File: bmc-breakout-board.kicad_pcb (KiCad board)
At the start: 4 copper layers, 90 x 60 mm, 49 parts, among them J1 PinHeader_2x4, J10 PinHeader_2x4, J11 PinHeader_2x05, J12 61300411121, J13 0473460001, J14 PCIE_BUS_x1, J15 0473460001, J16 PinHeader_1x07, J17 UE27AC54100, J2 PinHeader_2x13, J3 PinHeader_2x08, J4 61300411121, J5 ME1016813401101, J6 61300411121, J7 DC_SOCKET, J8 PinHeader_2x05, J9 PinHeader_1x07, Q1 SI2337DS, U1 FT234XD-R

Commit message: Bump revision to 1.0.1
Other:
- board text added: "DC-SCM Breakout Board Rev. 1.0.1"
- board text removed: "DC-SCM Breakout Board Rev. 1.0.0"
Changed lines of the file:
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@@
   (page A4)
   (layers
-    (0 F.Cu signal)
+    (0 F.Cu signal hide)
     (1 In1.Cu power hide)
     (2 In2.Cu power hide)
-    (31 B.Cu signal)
+    (31 B.Cu signal hide)
     (32 B.Adhes user hide)
     (33 F.Adhes user hide)
     (34 B.Paste user hide)
     (35 F.Paste user hide)
-    (36 B.SilkS user hide)
+    (36 B.SilkS user)
     (37 F.SilkS user)
     (38 B.Mask user hide)
-    (39 F.Mask user hide)
+    (39 F.Mask user)
     (40 Dwgs.User user hide)
     (41 Cmts.User user hide)
@@
   )
   (setup
-    (last_trace_width 1)
+    (last_trace_width 0.1)
     (user_trace_width 0.15)
     (user_trace_width 0.2)
@@
     (effects (font (size 1.5 1.5) (thickness 0.3)) (justify left))
   )
-  (gr_text "DC-SCM Breakout Board\nRev. 1.0.0" (at 90.535 105.45) (layer F.Mask)
+  (gr_text "DC-SCM Breakout Board\nRev. 1.0.1" (at 90.535 105.45) (layer F.Mask)
     (effects (font (size 1 1) (thickness 0.2)) (justify left))
   )

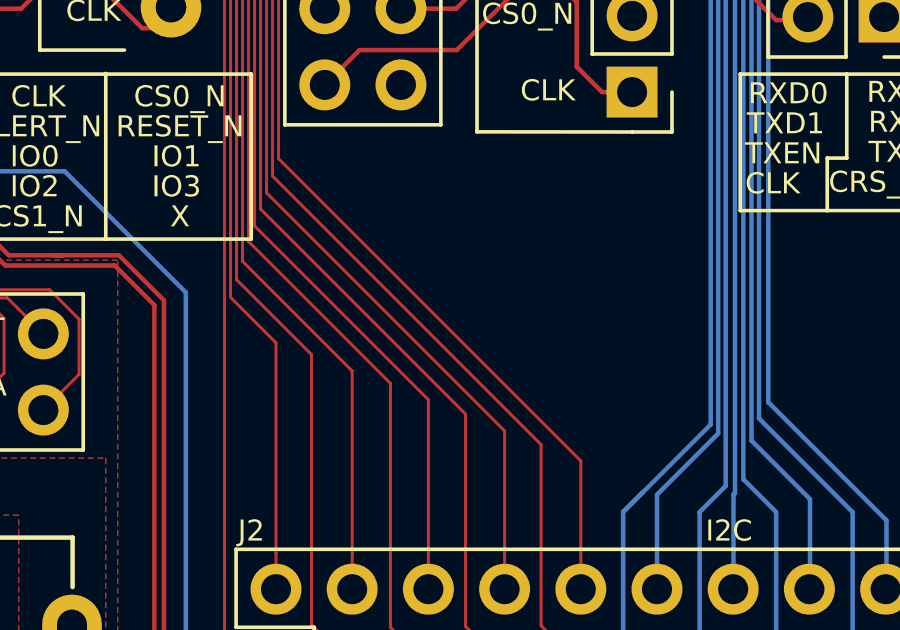
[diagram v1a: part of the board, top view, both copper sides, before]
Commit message: Fix logo position
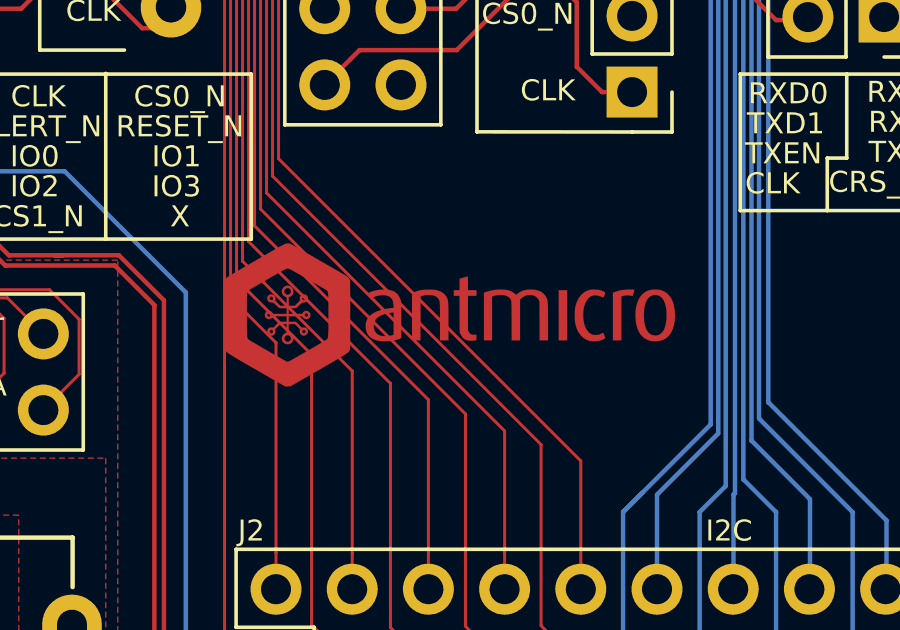
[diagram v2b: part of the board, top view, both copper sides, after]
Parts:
- N1: footprint bmc-breakout-board-footprints:antmicro-logo_scaled_20mm_mask -> antmicro-footprints:antmicro-logo_scaled_15mm
- moved N1 2.32 mm to (92.7, 101.0)

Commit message: Designator cleanup, DRC clean
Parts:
- moved N1 11.5 mm to (104.2, 102.2)
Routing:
- net GND: track 19.6 -> 33.2 mm, vias 29 -> 33
- net P12V_AUX: track 32.2 -> 42.5 mm, vias 10 -> 14
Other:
- board text removed: "I2C"

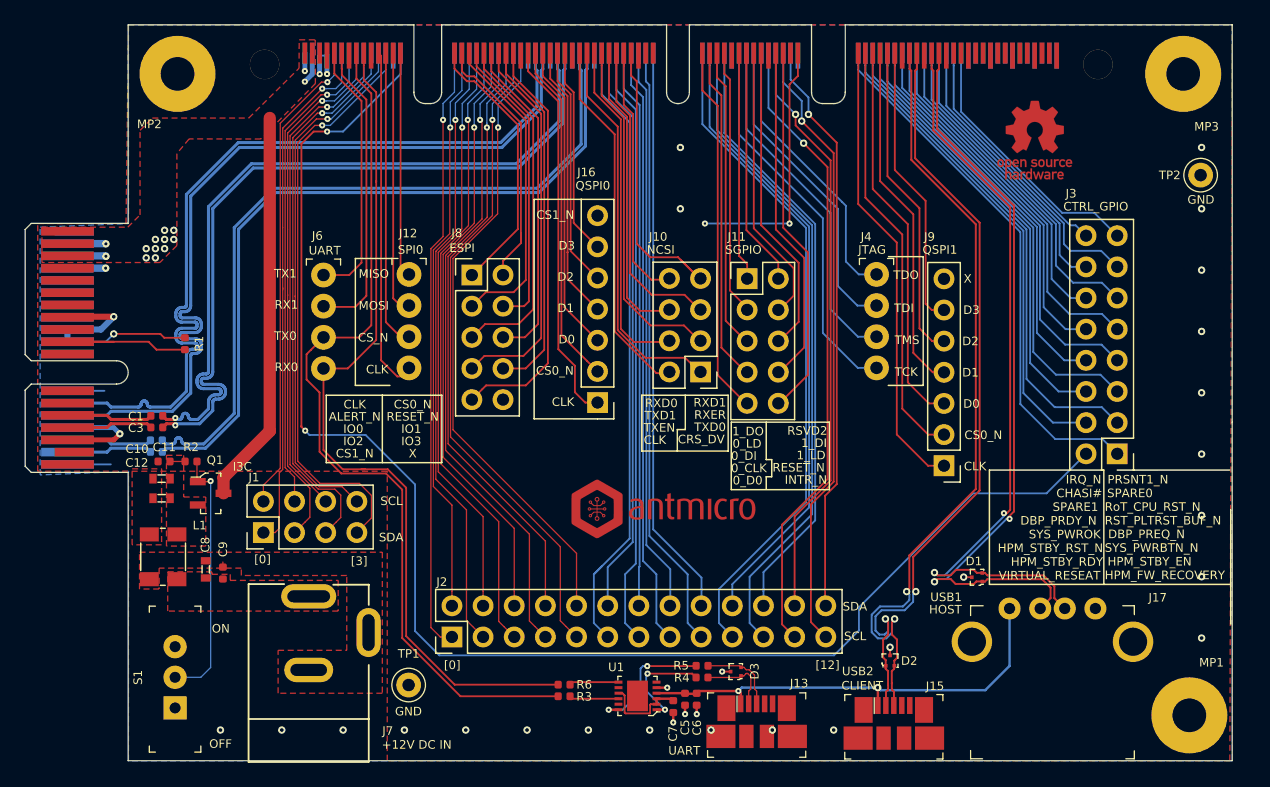
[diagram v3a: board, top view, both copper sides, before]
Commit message: Resize vias to be 0.6/0.25 DRC-Clean
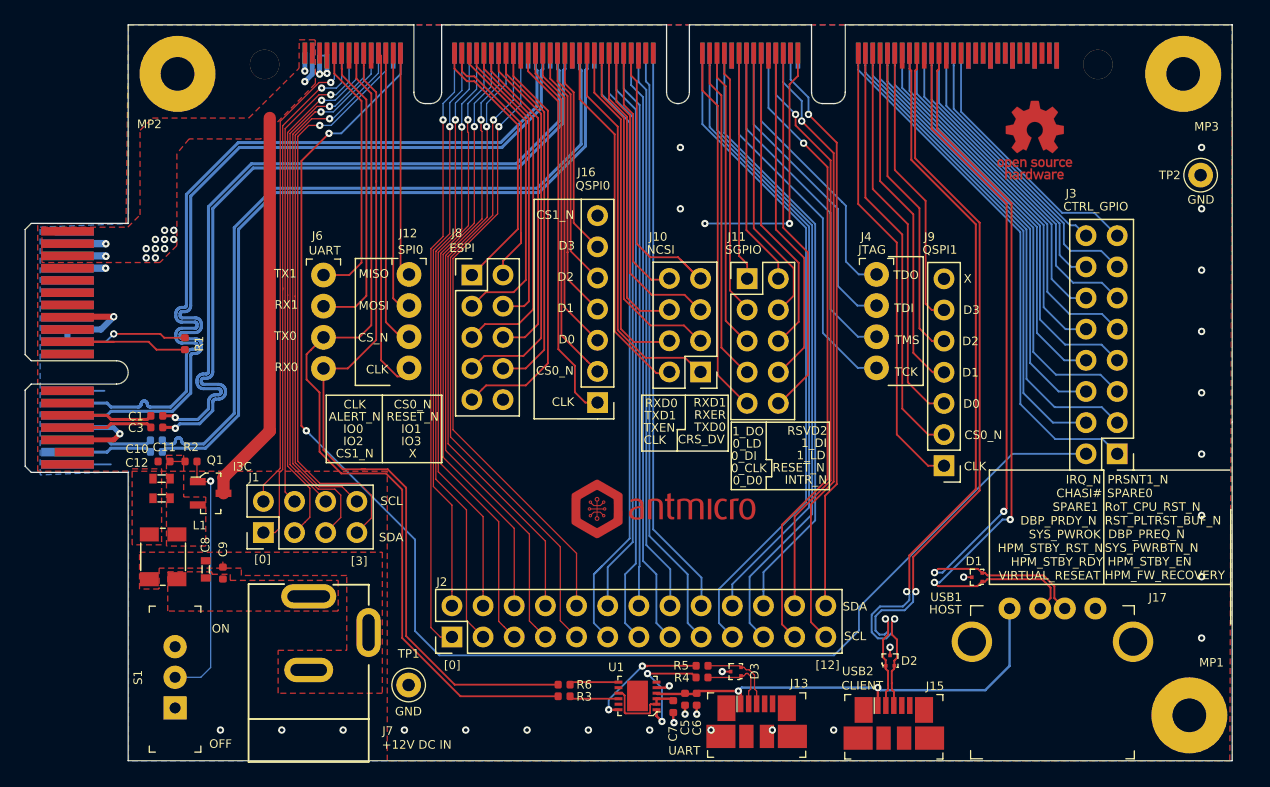
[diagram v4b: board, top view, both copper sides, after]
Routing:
- net VIRTUAL_RESEAT: track 121.8 -> 118.3 mm
- net Net-(R4-Pad2): track 8.40 -> 9.62 mm
- net USB1_D_P: track 61.3 -> 60.3 mm
- net /TX_P: track 61.4 -> 60.7 mm

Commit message: Add local lib
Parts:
- L1: footprint antmicro-footprints:744235900 -> bmc-breakout-board-footprints:744235900
- N1: footprint antmicro-footprints:antmicro-logo_scaled_15mm -> bmc-breakout-board-footprints:antmicro-logo_scaled_15mm
- N2: footprint antmicro-footprints:oshw-logo -> bmc-breakout-board-footprints:oshw-logo
- Q1: footprint antmicro-footprints:SOT-23-3 -> bmc-breakout-board-footprints:SOT-23-3
- S1: footprint antmicro-footprints:Switch_Slide_11.6x4mm_EG1218 -> bmc-breakout-board-footprints:Switch_Slide_11.6x4mm_EG1218
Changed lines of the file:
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@@
     )
   )
-  (module antmicro-footprints:antmicro-logo_scaled_15mm (layer F.Cu)
+  (module bmc-breakout-board-footprints:antmicro-logo_scaled_15mm (layer F.Cu)
     (at 104.17 102.205)
     (attr virtual)
@@
     )
   )
-  (module antmicro-footprints:744235900 (layer F.Cu)
+  (module bmc-breakout-board-footprints:744235900 (layer F.Cu)
     (at 62.9 106.065 90)
     (descr "Choke, Double, Doppeldrossel,  SMD, , Wuerth")
@@
     (pad 3 smd rect (at 1.85 -1.1 180) (size 1.55 1.15) (layers F.Cu F.Paste F.Mask)
       (net 1 GND))
-    (model ${KISYS3DMOD}/Inductor_SMD.3dshapes/L_Wuerth_WE-DD-Typ-L-Typ-XL-Typ-XXL.wrl
+    (model ${KIPRJMOD}/lib/3d-models/L_Wuerth_WE-DD-Typ-L-Typ-XL-Typ-XXL.wrl
       (at (xyz 0 0 0))
       (scale (xyz 1 1 1))
       (rotate (xyz 0 0 0))
     )
-    (model ${ANT3DMDL}/744235900.stp
+    (model ${KIPRJMOD}/lib/3d-models/744235900.stp
       (offset (xyz 0 0 2.75))
       (scale (xyz 1 1 1))
@@
     )
   )
-  (module antmicro-footprints:Switch_Slide_11.6x4mm_EG1218 (layer F.Cu)
+  (module bmc-breakout-board-footprints:Switch_Slide_11.6x4mm_EG1218 (layer F.Cu)
     (at 63.9 118.365 90)
     (descr http://spec_sheets.e-switch.com/specs/P040040.pdf)
@@
       (net 172 "Net-(S1-Pad1)"))
   )
-  (module antmicro-footprints:SOT-23-3 (layer F.Cu)
+  (module bmc-breakout-board-footprints:SOT-23-3 (layer F.Cu)
     (at 66.8 100.865)
     (attr smd)
@@
     (pad 3 smd rect (at 1.05 0) (size 1.3 0.6) (layers F.Cu F.Paste F.Mask)
       (net 49 P12V_AUX) (solder_mask_margin 0.07))
-    (model ${ANT3DMDL}/sot23-3.step
+    (model ${KIPRJMOD}/lib/3d-models/sot23-3.step
       (offset (xyz 0 0 0.35))
       (scale (xyz 1 1 1))
@@
     )
   )
-  (module antmicro-footprints:oshw-logo (layer F.Cu)
+  (module bmc-breakout-board-footprints:oshw-logo (layer F.Cu)
     (at 134 72.065)
     (attr virtual)
